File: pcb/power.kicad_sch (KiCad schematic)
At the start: 14 parts, among them IC1 LDFPVR, U1 7 -28 Vin 5 Vout

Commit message: pcb: wip
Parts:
- removed C2: 100n, symbol Device:C
- removed D1: 17V, symbol Device:D_TVS
- removed FB1: 120R @ 100 MHz, symbol Device:FerriteBead
- added C13, C14, C15, C16: 100uF, tractions_symbols:865080545012, symbol Device:C_Polarized
- added D3: SMBJ30CA, tractions_symbols:SMBJ33CA-824521331, symbol Device:D_TVS
- added L1: 1uH/24A, tractions_symbols:7443320100, symbol Device:L
- C1: footprint (none) -> Capacitor_SMD:C_0603_1608Metric
- C3: footprint (none) -> Capacitor_SMD:C_1206_3216Metric
- R1, R2: footprint (none) -> Resistor_SMD:R_0603_1608Metric
- U1: footprint (none) -> tractions_symbols:173950578
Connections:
- net VCCF is gone; now on net VCC: C3.1, U1.1 (VIN)
- net +5V: now also U1.3 (VOUT); no longer U1. (VOUT)
- net GND: now also U1.2 (GND), C13.2, C14.2, C15.2, C16.2, D3.1 (A1); no longer U1. (VOUT)
- net VCC: now also C13.1, C15.1, C16.1, L1.2
- new net +VDC: C14.1, D3.2 (A2), L1.1
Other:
- note removed: "742692003"
- note removed: "82306050029"
- company: (none) -> ProMez - David Mezler
- title: (none) -> TractionHub V1
- moved on the sheet: C1, C3, C4, C5, C6, IC1, R1, R2, R3, R4

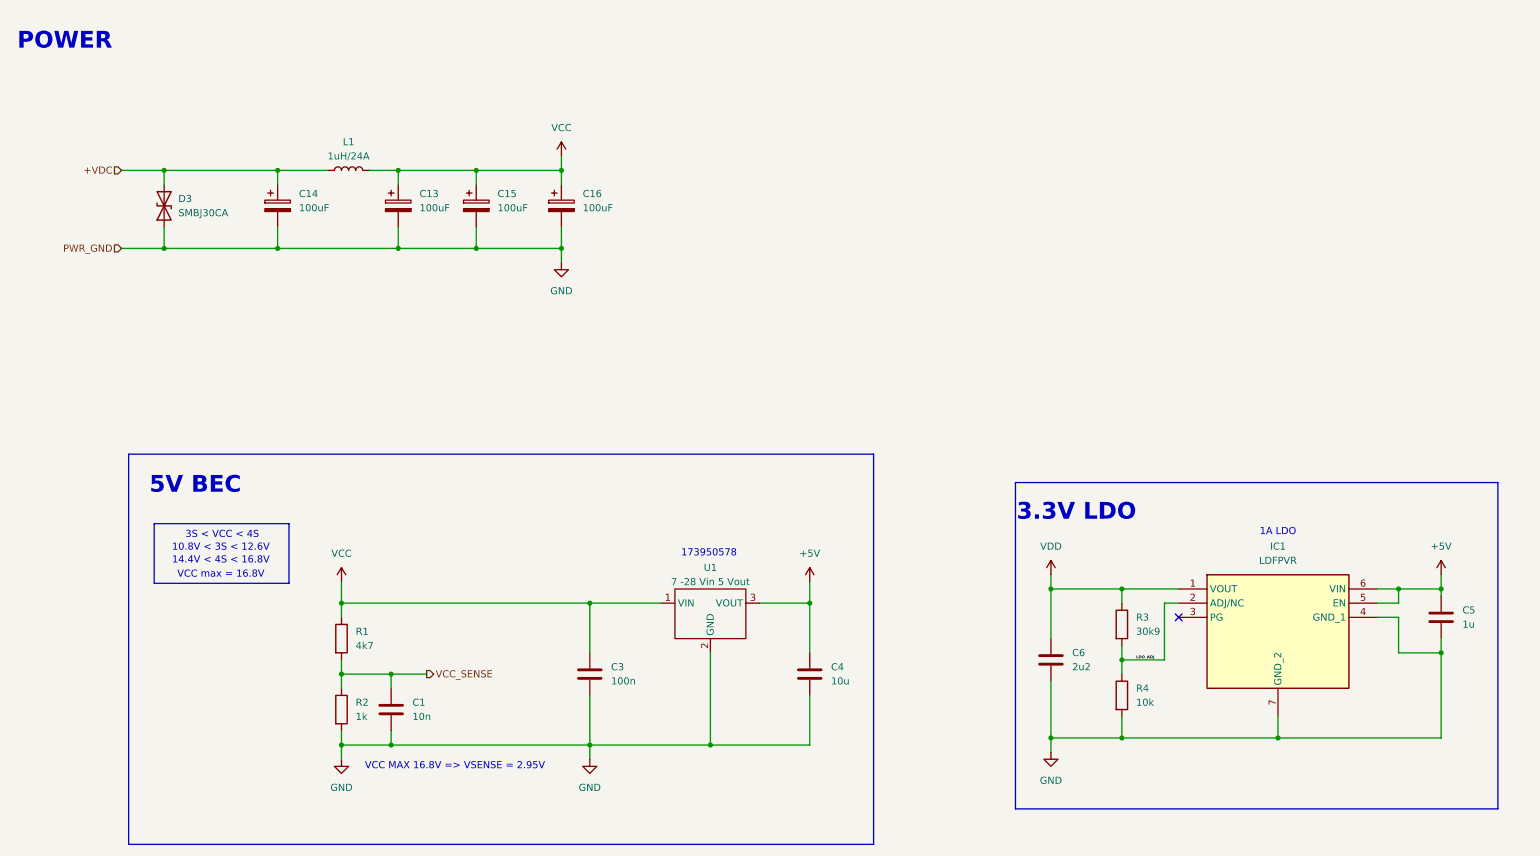
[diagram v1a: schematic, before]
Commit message: pcb: first version schematic
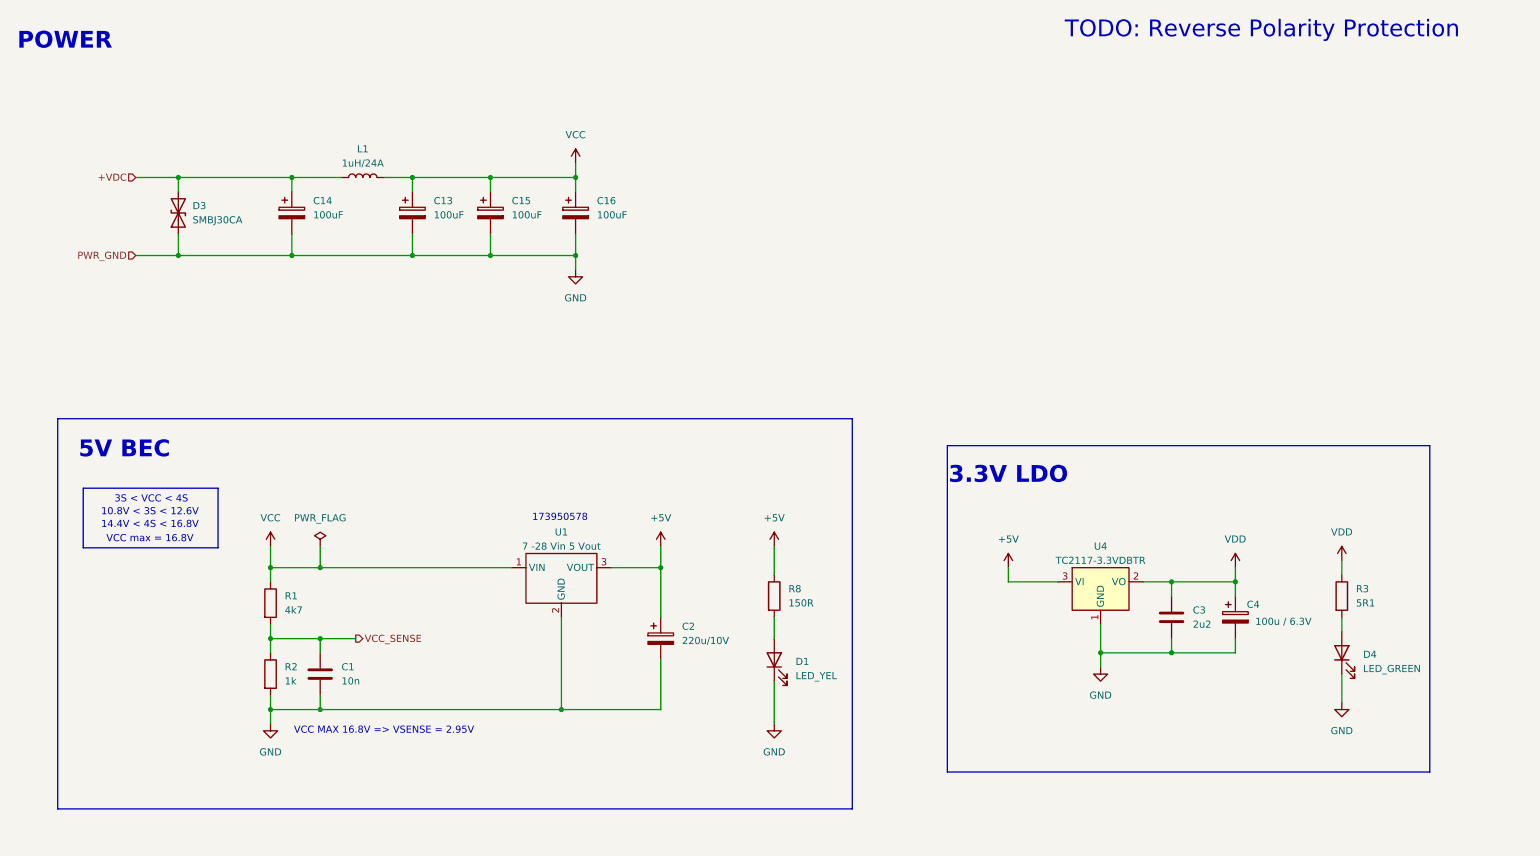
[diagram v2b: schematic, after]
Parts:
- removed C4: 10u, symbol Device:C
- removed C5: 1u, symbol Device:C
- removed C6: 2u2, symbol Device:C
- removed IC1: LDFPVR, SON65P200X200X100-7N-D, symbol traction_symbols:LDFPVR
- removed R4: 10k, symbol Device:R
- added C2: 220u/10V, tractions_symbols:865080545012, symbol Device:C_Polarized
- added C4: 100u / 6.3V, tractions_symbols:865080142007, symbol Device:C_Polarized
- added D1: LED_YEL, LED_SMD:LED_0603_1608Metric, symbol Device:LED
- added D4: LED_GREEN, LED_SMD:LED_0603_1608Metric, symbol Device:LED
- added R8: 150R, Resistor_SMD:R_0603_1608Metric, symbol Device:R
- added U4: TC2117-3.3VDBTR, Package_TO_SOT_SMD:SOT-223-3_TabPin2, symbol traction_symbols:TC2117
- C3: value 100n -> 2u2; footprint Capacitor_SMD:C_1206_3216Metric -> Capacitor_SMD:C_0603_1608Metric
- R3: value 30k9 -> 5R1; footprint (none) -> Resistor_SMD:R_0603_1608Metric
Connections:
- net +5V: now also C2.1, R8.1, U4.3 (VI)
- net GND: now also C2.2, C4.2, D1.1 (K), D4.1 (K), U4.1 (GND)
- net VCC: no longer C3.1
- net VDD: now also C3.1, C4.1, U4.2 (VO)
- net LDO_ADJ: no longer names the net of R3.2
- net LDO_ADJ: now also D4.2 (A)
- new net: D1.2 (A), R8.2
- no-connect marks 1 -> 0
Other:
- note added: "TODO: Reverse Polarity Protection"
- note removed: "1A LDO"
- moved on the sheet: C1, C13, C14, C15, C16, D3, L1, R1, R2, U1

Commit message: pcb: complete bom and first layout
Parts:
- C1: value 10n -> 100nF
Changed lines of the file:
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@@
 			)
 		)
-		(property "Value" "10n"
+		(property "Value" "100nF"
 			(at 74.93 134.6199 0)
 			(effects

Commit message: pcb: layout gate driver
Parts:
- U4: value TC2117-3.3VDBTR -> TC2117-3.3VDBTR
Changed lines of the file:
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@@
 			)
 		)
-		(property "Value" "TC2117-3.3VDBTR "
+		(property "Value" "TC2117-3.3VDBTR"
 			(at 210.82 113.03 0)
 			(effects
